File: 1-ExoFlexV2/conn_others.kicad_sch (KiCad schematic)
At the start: 13 parts, among them J56 4, J57 3, J58 3

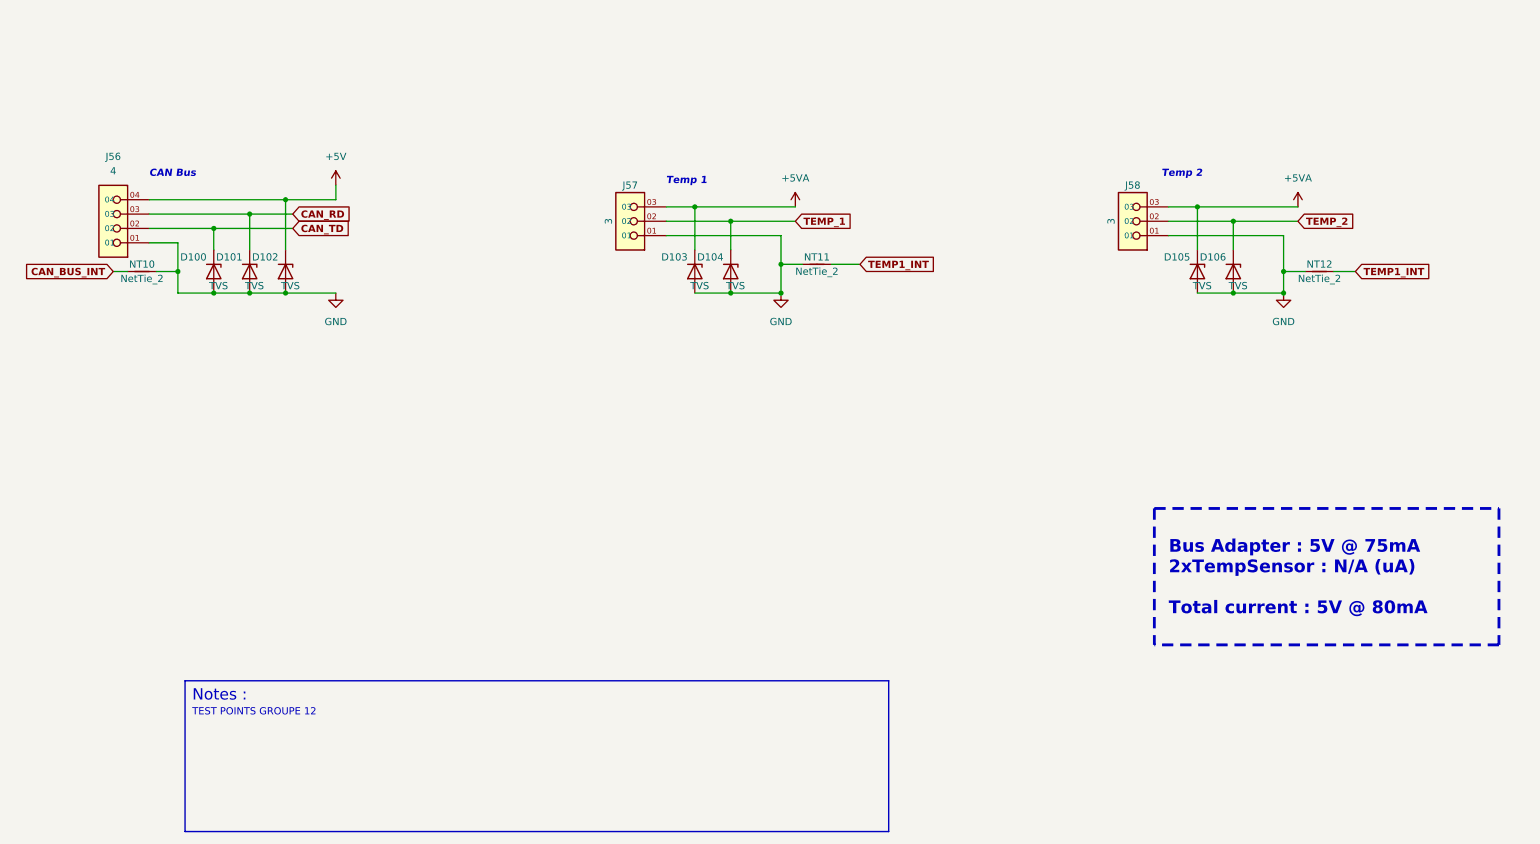
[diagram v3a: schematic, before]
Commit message: Finalisation 3
- Changement des régulateur de tension
- Retrait de test point inutile
- Changement de jumper mal positionner
- Ajout de Mounting holes et fiducial
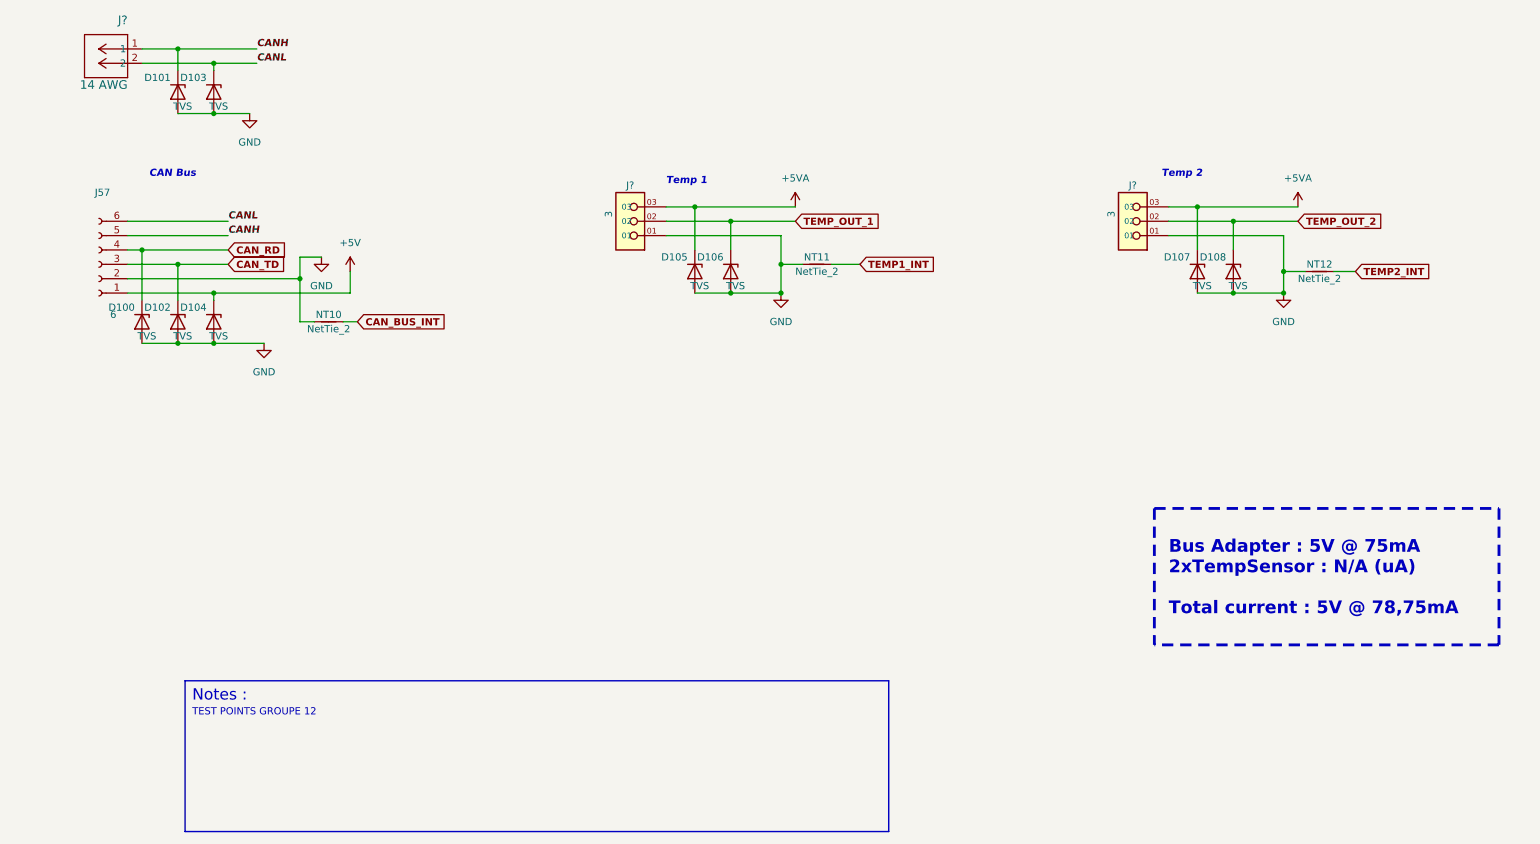
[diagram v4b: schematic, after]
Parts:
- removed J56: 4, FootPrint:PHOENIX_1751112, symbol SymLib:1751112
- removed J57, J58: 3, FootPrint:PHOENIX_1751109, symbol SymLib:1751109
- added D103, D104: TVS, FootPrint:DPY2_TEX, symbol Device:D_Zener
- added J57: 6, Connector_PinSocket_2.54mm:PinSocket_1x06_P2.54mm_Vertical, symbol Connector:Conn_01x06_Female
- added J? (x2): 3, FootPrint:PHOENIX_1755749, symbol SymLib:1751109
- added J?: 14 AWG, FootPrintLib:PHOENIX_1755736, symbol SymLib:1729128
- renumbered D103 to D105, D104 to D106, D105 to D107, D106 to D108
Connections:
- net +5V: now also D104.1 (K), J57.1 (Pin_1); no longer D102.1 (K)
- net +5VA: now also J?.03, J?.03
- net CAN_RD: now also D100.1 (K), J57.4 (Pin_4); no longer D101.1 (K)
- net CAN_TD: now also D102.1 (K), J57.3 (Pin_3); no longer D100.1 (K)
- net GND: now also D103.2 (A), D104.2 (A), J57.2 (Pin_2), J?.01, J?.01
- net TEMP1_INT: no longer NT12.2
- net TEMP_1 renamed TEMP_OUT_1
- net TEMP_OUT_1: now also J?.02
- net TEMP_2 renamed TEMP_OUT_2
- net TEMP_OUT_2: now also J?.02
- new net CANH: D101.1 (K), J57.5 (Pin_5), J?.1
- new net CANL: D103.1 (K), J57.6 (Pin_6), J?.2
- new net TEMP2_INT: NT12.2
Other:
- note added: "Bus Adapter : 5V @ 75mA 2xTempSensor : N/A (uA) Total current : 5V @ 78,75mA"
- note removed: "Bus Adapter : 5V @ 75mA 2xTempSensor : N/A (uA) Total current : 5V @ 80mA"

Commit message: Finalisation schéma FIN
- Changement des uméro pour les inverseurs
- Changement des connecteur et début de placement
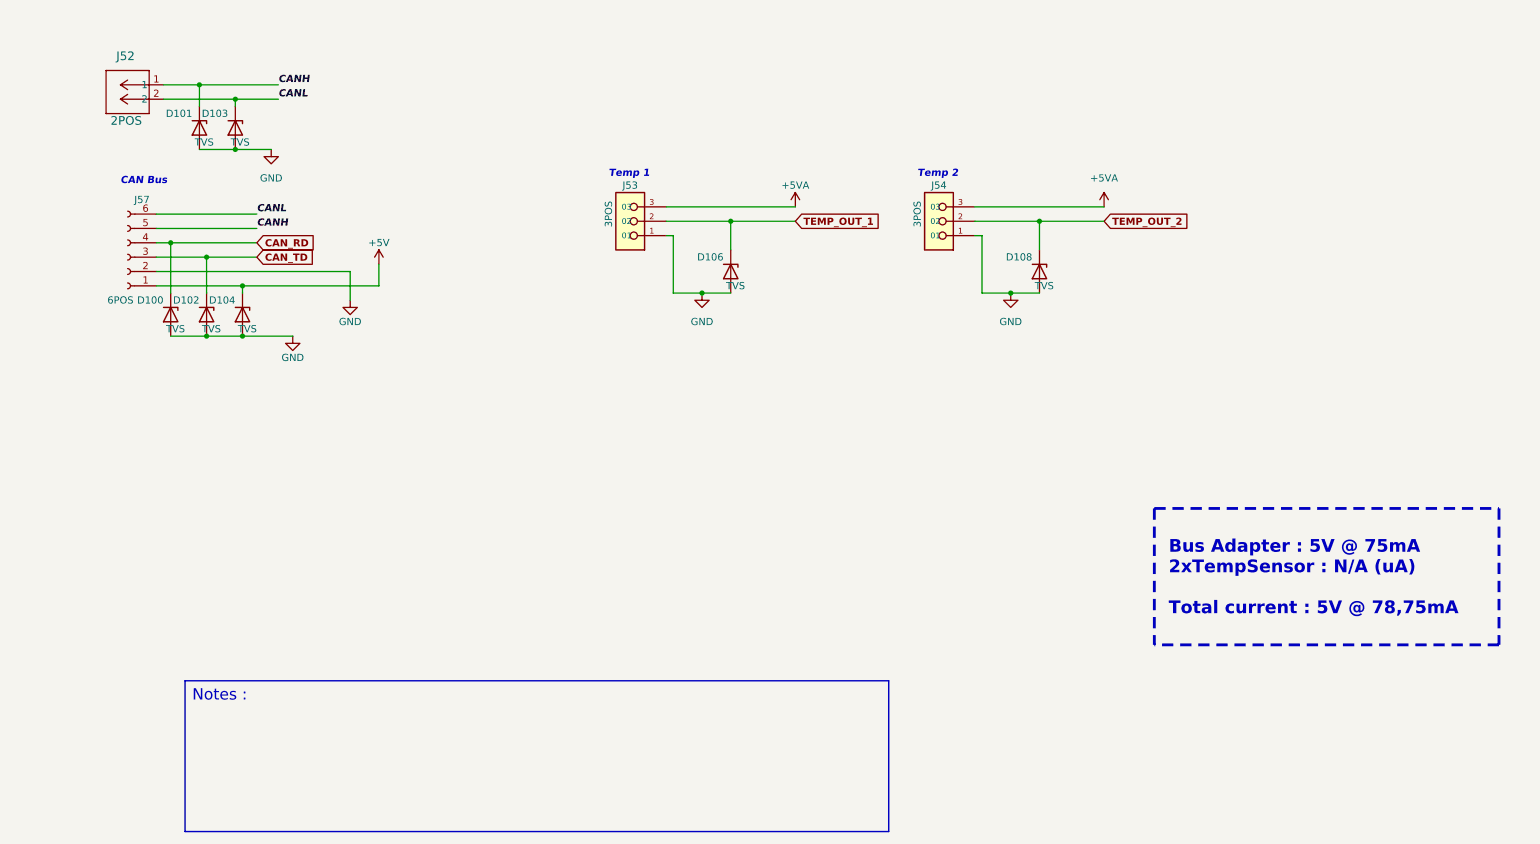
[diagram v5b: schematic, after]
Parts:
- removed D105, D107: TVS, FootPrint:DPY2_TEX, symbol Device:D_Zener
- removed J?: 14 AWG, FootPrintLib:PHOENIX_1755736, symbol SymLib:1729128
- removed NT10, NT11, NT12: NetTie_2, NetTie:NetTie-2_SMD_Pad0.5mm, symbol Device:NetTie_2
- added J52: 2POS, FootPrintLib:CON_39281023, symbol SymLib:1729128
- J53, J54: renamed from J?; value 3 -> 3POS; footprint FootPrint:PHOENIX_1755749 -> FootPrint:CON_39301039; DESCRIPTION 3 Position Terminal Block Header, Male Pins, Shrouded (4 Si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 -> Connector Header Through Hole 3 position 0.165" (4.20mm); MANUFACTURER Phoenix Contact -> Molex; PACKAGE 3 POS 0.200" (5.08mm) -> 3 POS 0.165" (4,2mm); PART NUMBER 1755749 -> 0039301039
- J57: value 6 -> 6POS
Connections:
- net +5VA: now also J53.3 (03), J54.3 (03); no longer J53.03, J54.03
- net CANH: now also J52.1
- net CANL: now also J52.2
- net GND: now also J53.1 (01), J54.1 (01); no longer J53.01, J54.01
- net TEMP_OUT_1: now also J53.2 (02); no longer J53.02
- net TEMP_OUT_2: now also J54.2 (02); no longer J54.02
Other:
- note removed: "TEST POINTS GROUPE 12"
- moved on the sheet: D100, D101, D102, D103, D104, D108, J54, J57

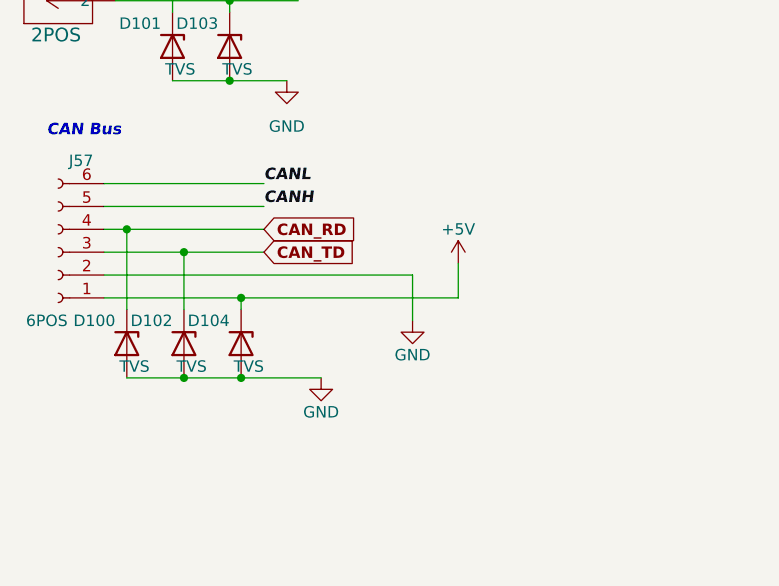
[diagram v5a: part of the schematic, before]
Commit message: Routage pour Review 1
- Replacement des test point pour faciliter le rework
- Correction des erreurs dans le BOM
-
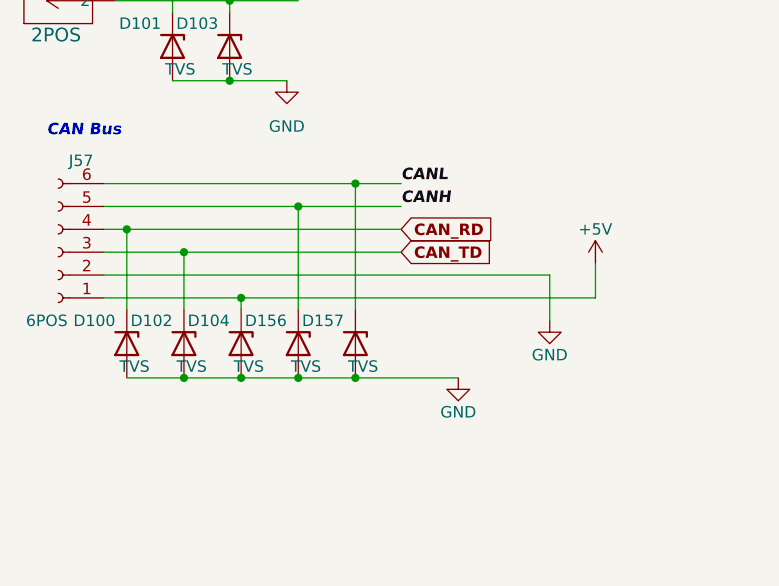
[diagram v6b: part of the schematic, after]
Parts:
- added D156, D157: TVS, FootPrint:DPY2_TEX, symbol Device:D_Zener
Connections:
- net CANH: now also D156.1 (K)
- net CANL: now also D157.1 (K)
- net GND: now also D156.2 (A), D157.2 (A)
